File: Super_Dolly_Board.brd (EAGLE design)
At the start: 154.5 x 45 mm, 101 parts, among them J1 10118193-0001LF, J3 SJ1-2503A, J4 RJHSE-5381, J5 SJ1-2503A, J6 SJ1-2503A, P1 TC33X-2, SW1 SKQUDBE010, U1 AT90USB646-MU, U10 IP4234CZ6, U11 AT90USB646-AU, U2 MMDT3904, U3 BTM7755, U4 TS2937CW50, U6 ISL8483, U9 TS2937CW50, X1 3.2X2.5MMCRYSTAL

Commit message: Tagged SDB REV_3
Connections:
- net N$1 renamed M0_A1
- net N$2 renamed M0_B1
- net N$3 renamed M0_P1
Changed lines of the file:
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@@
 <wire x1="-5.277440625" y1="3.527440625" x2="-2.97255625" y2="3.527440625" width="0.254" layer="1"/>
 <wire x1="-2.97255625" y1="3.527440625" x2="-2.70961875" y2="3.790378125" width="0.254" layer="1"/>
-<wire x1="-11.161521875" y1="2.1923875" x2="-11.161521875" y2="2.088478125" width="0" layer="19" extent="1-1"/>
+<wire x1="-11.161521875" y1="2.088478125" x2="-11.161521875" y2="2.1923875" width="0.254" layer="1"/>
 </signal>
 <signal name="N$5">
@@
 <wire x1="-21.891865625" y1="-6.5934125" x2="-22.758071875" y2="-5.72720625" width="0.1778" layer="1"/>
 </signal>
-<signal name="N$3">
+<signal name="M0_P1">
 <contactref element="R26" pad="1"/>
 <contactref element="U5" pad="27"/>
@@
 <wire x1="49.100003125" y1="-10.65" x2="49.100003125" y2="-8.135" width="0.254" layer="16"/>
 </signal>
-<signal name="N$1">
+<signal name="M0_A1">
 <contactref element="R7" pad="1"/>
 <contactref element="U5" pad="10"/>
@@
 <wire x1="26.85" y1="-19.65" x2="26.85" y2="-17.865" width="0.254" layer="16"/>
 </signal>
-<signal name="N$2">
+<signal name="M0_B1">
 <contactref element="R8" pad="1"/>
 <contactref element="U5" pad="9"/>
@@
 <wire x1="-3.5" y1="2.75" x2="-6.75" y2="-0.5" width="0.254" layer="1"/>
 <wire x1="-6.75" y1="-0.5" x2="-7" y2="-0.5" width="0.254" layer="1"/>
-<wire x1="-7" y1="-0.5" x2="-8" y2="-1.5" width="0.254" layer="1"/>
+<wire x1="-7" y1="-0.5" x2="-7.875" y2="-1.375" width="0.254" layer="1"/>
+<wire x1="-7.875" y1="-1.375" x2="-8" y2="-1.5" width="0.254" layer="1"/>
 <wire x1="2.75" y1="2.5" x2="11" y2="2.5" width="0.254" layer="1"/>
 <via x="14.75" y="2.5" extent="1-16" drill="0.6"/>
@@
 <wire x1="10.75" y1="2.85" x2="11" y2="2.6" width="0.254" layer="1"/>
 <wire x1="11" y1="2.6" x2="11" y2="2.5" width="0.254" layer="1"/>
-<wire x1="-8" y1="-1.5" x2="-7.767409375" y2="-1.41385625" width="0" layer="19" extent="1-1"/>
+<wire x1="-7.767409375" y1="-1.41385625" x2="-7.875" y2="-1.41385625" width="0.254" layer="1"/>
+<wire x1="-7.875" y1="-1.41385625" x2="-7.875" y2="-1.375" width="0.254" layer="1"/>
 </signal>
 <signal name="PE2">

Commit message: working on SDB REV4
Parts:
- added AUX_2: (no value), PP_Connectors:HEADER_01X08_1.27_PTH
- R3, R32, R6: value 10K -> 4.7K
- moved R29 10.8 mm to (-22.8, -19.7)
- moved CG10 8.84 mm to (19.5, 4.75), turned to 90 degrees
- moved R32 8.00 mm to (-18.2, -19.7)
- moved R26 5.25 mm to (-13.8, -19.8)
- moved R7 3.50 mm to (-10.2, -19.8)
- moved R8 3.25 mm to (-12.0, -19.8)
- moved R3 1.50 mm to (-15.2, -19.8)
- moved R6 1.50 mm to (-16.8, -19.7)
- moved H1 1.25 mm to (-69.5, -22.2)
- moved C12 0.50 mm to (75.5, -22.0)
- moved LOGO2 0.25 mm to (-51.8, -11.0)
- renumbered AUX to AUX_1
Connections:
- new net N$2: AUX_2.P$3
- net +5V: now also AUX_2.P$1
- net GND: now also AUX_2.P$2; no longer CG10.1
- net M0_A: now also U1.51, U11.51; no longer U1.48, U11.48
- net M0_B: now also U1.50, U11.50; no longer U1.47, U11.47
- net M0_P: now also U1.49, U11.49; no longer U1.51, U11.51
- net M1_A: now also U1.48, U11.48; no longer U1.46, U11.46
- net M1_B: now also U1.47, U11.47; no longer U1.45, U11.45
- net M1_P: now also U1.46, U11.46; no longer U1.50, U11.50
- net M2_A: now also U1.45, U11.45; no longer U1.44, U11.44
- net M2_B: now also U1.44, U11.44; no longer U1.10, U11.10
- net M2_P: now also U1.10, U11.10; no longer U1.49, U11.49
- net PD5: now also AUX_2.P$4
- net PD6: now also AUX_2.P$5
- net PD7: now also AUX_2.P$6
- net PE0: now also AUX_2.P$7
- net PE1: now also AUX_2.P$8
- net PF5: now also U3.28
- net PF6: now also U7.28
- net PF7: now also U5.28
- net UGND: now also CG10.1
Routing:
- net PD5: track 4.17 -> 43.3 mm
- net M2_P: track 6.87 -> 44.6 mm, vias 0 -> 2
- net PD6: track 4.28 -> 41.2 mm
- net PD7: track 4.41 -> 38.9 mm
- net PE0: track 4.42 -> 36.6 mm
- net M2_B: track 42.7 -> 11.0 mm, vias 2 -> 0
- net PE1: track 4.28 -> 35.5 mm
- net N$8: track 91.6 -> 111.8 mm
- net N$7: track 68.4 -> 85.2 mm
- net M0_P1: track 44.1 -> 57.2 mm
- net M0_B1: track 48.2 -> 43.6 mm
- net M0_A1: track 44.2 -> 39.6 mm
- net +5V: track 514.7 -> 518.2 mm
- net UGND: track 66.6 -> 69.1 mm
- net N$4: track 70.3 -> 68.0 mm
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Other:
- board size 154.5 x 45 mm -> 154.5 x 45.8 mm
- board text added: "(c) Copyright 2013"
- board text added: "Super Dolly Board REV 4"
- board text removed: "(c) Copyright 2012"
- board text removed: "Super Dolly Board REV 3"

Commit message: working on REv 4 of SDB
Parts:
- removed C20: 10uF, SparkFun:EIA3216
- removed U9: TS2937CW50, SparkFun-PowerIC:SOT223
- added C22, C23: .1uF, parkers_parts:0402_CAP
- added R35: 20K, parkers_parts:0402_RES
- added R36: LRF1206-LF-R006JT, PP_Passives:1206
- added R37: 10K, parkers_parts:0402_RES
- added U12: BSO080P03NS3E G, PP_DiscreteSemi:DSO-8
- added U8: LMP8640MK-H/NOPB, PP_AnalogIC:TSOT-6
- D1: value PMEG6010EP -> MMSZ5240C-V-GS08; device parkers_parts:SOD-128 -> parkers_parts:SOD-123
- D2: value PMEG6010EP -> PMEG4010EP,115
- moved U$1 140.7 mm to (31.3, 5.25)
- moved D1 9.28 mm to (-64.0, -5.00), turned to 0 degrees
- moved LOGO2 4.03 mm to (-49.8, -7.50)
- moved D2 3.47 mm to (-54.0, 1.00), turned to 90 degrees
- moved CG5 0.25 mm to (-31.2, 6.75)
- moved OK1 0.25 mm to (-32.8, 2.37)
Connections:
- new net N$1: R35.2, U8.1
- new net N$3: D1.ANODE, R37.2, U12.4
- new net VIN_J: PWR.PWR, U12.5, U12.6, U12.7, U12.8
- new net VIN_M: C10.2, C11.2, C12.POS, C9.2, R36.2, U3.11, U3.12, U3.13, U3.14, U3.29, U3.30, U3.31, U3.32, U5.11, U5.12, U5.13, U5.14, U5.29, U5.30, U5.31, U5.32, U7.11, U7.12, U7.13, U7.14, U7.29, U7.30, U7.31, U7.32, U8.4
- net +5V: now also C22.2, U8.6; no longer U9.3
- net 12VB: now also D2.ANODE; no longer C20.A, D2.CATHODE, U9.1
- net GND: now also C22.1, C23.1, R37.1, U8.2; no longer C20.C, D1.ANODE, D2.ANODE, U9.2
- net PF2: now also C23.2, R35.1
- net PF5: no longer U3.28
- net PF6: no longer U7.28
- net PF7: no longer U5.28
- net VIN: now also D2.CATHODE, R36.1, U12.1, U12.2, U12.3, U8.3; no longer C10.2, C11.2, C12.POS, C9.2, PWR.PWR, U3.11, U3.12, U3.13, U3.14, U3.29, U3.30, U3.31, U3.32, U5.11, U5.12, U5.13, U5.14, U5.29, U5.30, U5.31, U5.32, U7.11, U7.12, U7.13, U7.14, U7.29, U7.30, U7.31, U7.32
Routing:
- net VIN: track 344.7 -> 62.2 mm, vias 2 -> 7
- net VIN_M: track 0.00 -> 105.4 mm, vias 0 -> 2
- net +5V: track 518.2 -> 504.7 mm, vias 10 -> 11
- net GND: track 48.6 -> 39.6 mm, vias 71 -> 44
- net 12VB: track 33.0 -> 24.5 mm
- net N$1: track 0.00 -> 7.48 mm
- net PF2: track 27.3 -> 33.4 mm
- net N$3: track 0.00 -> 4.21 mm
- added copper zone on layer 1, net VIN
- added copper zone on layer 16, net VIN
- added copper zone on layer 1, net VIN_J
- added copper zone on layer 16, net VIN_M

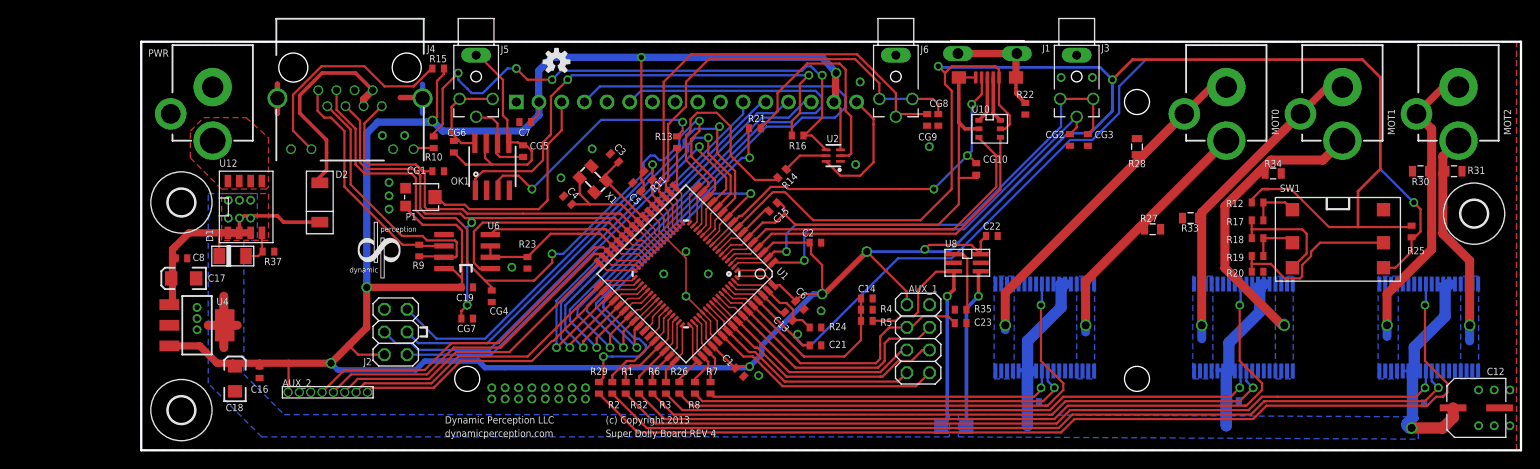
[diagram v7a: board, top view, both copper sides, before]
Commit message: added a new PP_Sensor library and more parts to the datasheets
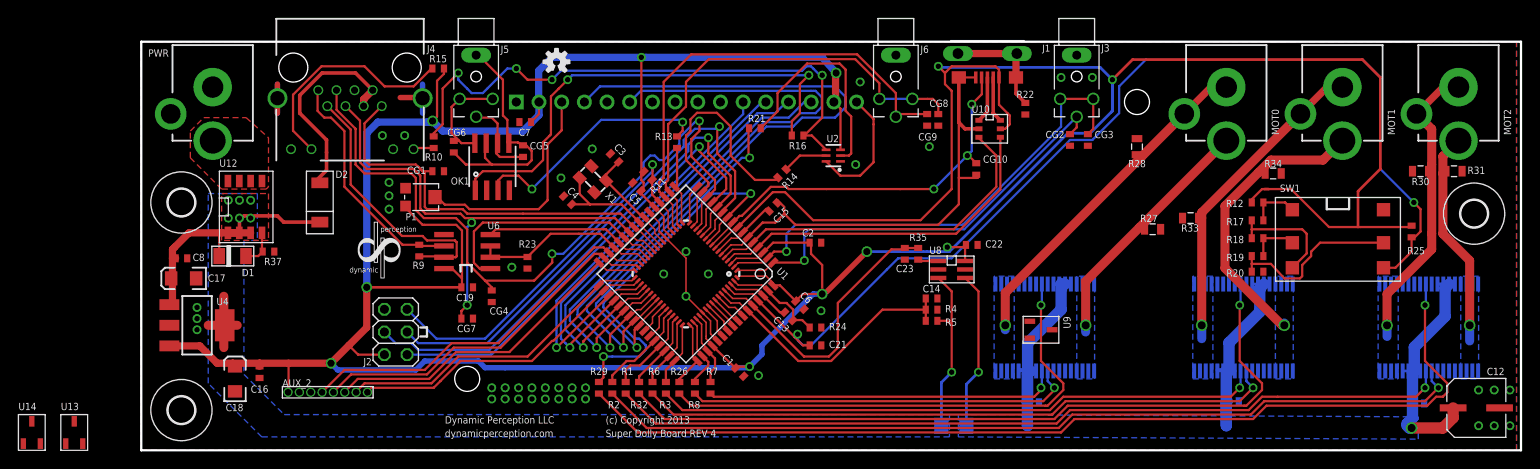
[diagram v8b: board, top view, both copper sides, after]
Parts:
- removed AUX_1: (no value), pinhead:2X04
- added U13, U14, U9: MCP9701T-E/TT, PP_Sensors:SOT-23-3
- moved LOGO1 21.0 mm to (44.5, -7.75)
- moved C23 9.96 mm to (11.5, -4.75), turned to 90 degrees
- moved R35 7.85 mm to (13.0, -4.75), turned to 270 degrees
- moved C14 7.25 mm to (14.5, -9.75)
- moved R4 7.25 mm to (14.5, -11.0)
- moved R5 7.25 mm to (14.5, -12.2)
- moved C22 2.46 mm to (19.0, -3.75)
- moved U8 1.90 mm to (16.8, -6.50)
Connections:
- removed net BATT_V: C14.1, R4.2, R5.1, U1.60, U11.60
- removed net PF2: AUX_1.3, C23.2, R35.1, U1.59, U11.59
- removed net PF3: AUX_1.4, U1.58, U11.58
- removed net PF4: AUX_1.5, U1.57, U11.57
- removed net PF5: AUX_1.6, U1.56, U11.56
- new net CUR_SENSOR: C23.2, R35.1, U1.60, U11.60
- new net TEMP0_SENSOR: U1.56, U11.56, U9.2
- new net TEMP1_SENSOR: U1.57, U11.57, U13.2
- new net TEMP2_SENSOR: U1.58, U11.58, U14.2
- new net VOL_SENSOR: C14.1, R4.2, R5.1, U1.59, U11.59
- net +5V: now also U13.1, U14.1, U9.1; no longer AUX_1.1
- net GND: now also U13.3, U14.3, U9.3; no longer AUX_1.2
- net PF6: no longer AUX_1.7
- net PF7: no longer AUX_1.8
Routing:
- net PF2: track 33.4 -> 0.00 mm
- net CUR_SENSOR: track 0.00 -> 32.8 mm
- net VOL_SENSOR: track 0.00 -> 30.9 mm
- net PF3: track 30.1 -> 0.00 mm
- net PF5: track 29.2 -> 0.00 mm
- net PF7: track 29.9 -> 3.80 mm
- net PF4: track 25.9 -> 0.00 mm
- net BATT_V: track 23.9 -> 0.00 mm
- net PF6: track 26.5 -> 3.66 mm
- net +5V: track 504.7 -> 491.5 mm
- net VIN: track 62.2 -> 51.8 mm
- net N$1: track 7.48 -> 2.31 mm
- net TEMP2_SENSOR: track 0.00 -> 3.69 mm
- net TEMP0_SENSOR: track 0.00 -> 3.54 mm
- net TEMP1_SENSOR: track 0.00 -> 3.54 mm
